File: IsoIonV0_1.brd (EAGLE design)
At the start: 41.9 x 27.9 mm, 56 parts, among them IC1 MCP3221, IC2 MCP4017-100K, IC4 TL072, IC5 TPS60400DBV

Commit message: Cleaned up sch small silkscreen adjustment on brd
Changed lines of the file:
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@@
 <wire x1="28.702" y1="22.606" x2="28.702" y2="19.558" width="0.8128" layer="21"/>
 <wire x1="28.702" y1="27.432" x2="28.702" y2="10.668" width="0.8128" layer="22" style="shortdash"/>
-<wire x1="28.702" y1="16.51" x2="28.702" y2="13.97" width="0.8128" layer="21" style="longdash"/>
+<wire x1="28.702" y1="16.51" x2="28.702" y2="14.224" width="0.8128" layer="21" style="longdash"/>
 </plain>
 <attributes>
@@
 </signal>
 </signals>
-<errors>
-</errors>
 </board>
 </drawing>

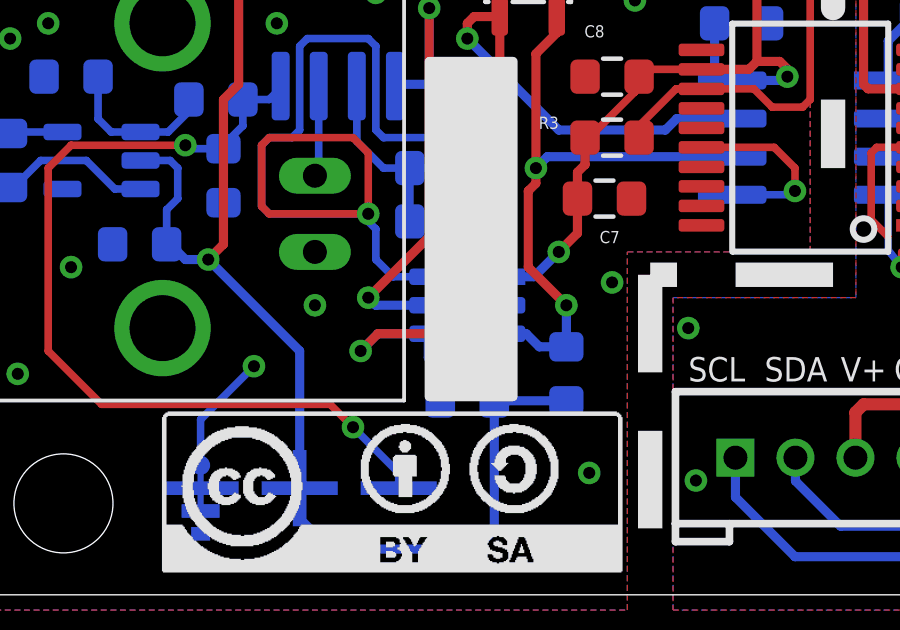
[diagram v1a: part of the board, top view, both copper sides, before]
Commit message: MCP4017 package updated to SC70-6
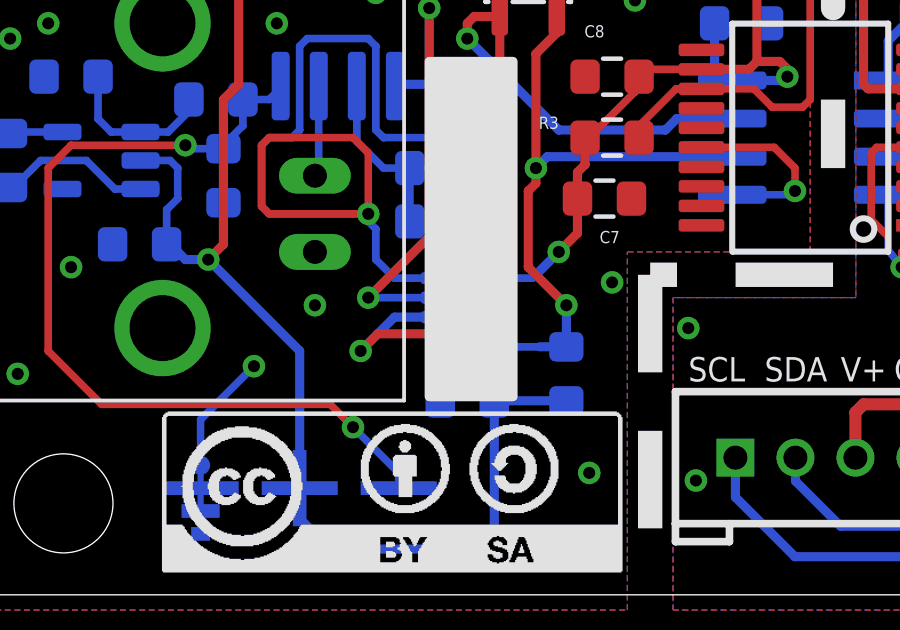
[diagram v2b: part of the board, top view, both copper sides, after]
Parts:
- IC2: device SW_DigitalAnalogICs:SOT23-6 -> SW_DigitalAnalogICs:SC70
- moved IC2 0.25 mm to (16.5, 9.91)
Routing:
- net ISOSDA: track 30.9 -> 31.8 mm
- net ISOSCL: track 20.8 -> 21.5 mm
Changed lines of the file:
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@@
 <attribute name="VALUE" x="16.764" y="27.305" size="0.4064" layer="28" rot="MR0"/>
 </element>
-<element name="IC2" library="SW_DigitalAnalogICs" package="SOT23-6" value="MCP4017-100K" x="16.51" y="9.652" smashed="yes" rot="MR270"/>
+<element name="IC2" library="SW_DigitalAnalogICs" package="SC70" value="MCP4017-100K" x="16.51" y="9.906" smashed="yes" rot="MR270"/>
 <element name="ISOIC1" library="SparkysWidgets" package="SO08" value="ADUM1250" x="27.94" y="15.24" smashed="yes" rot="MR270"/>
 <element name="ISOIC2" library="SparkysWidgets" package="SSOP20" value="ADUM6010" x="27.94" y="15.24" smashed="yes" rot="R90"/>
@@
 <wire x1="13.081" y1="12.573" x2="13.462" y2="12.192" width="0.254" layer="16"/>
 <wire x1="13.462" y1="12.192" x2="13.462" y2="11.176" width="0.254" layer="16"/>
-<wire x1="13.462" y1="11.176" x2="14.036" y2="10.602" width="0.254" layer="16"/>
-<wire x1="15.21" y1="10.602" x2="14.036" y2="10.602" width="0.254" layer="16"/>
+<wire x1="13.462" y1="11.176" x2="14.082" y2="10.556" width="0.254" layer="16"/>
 <wire x1="14.594" y1="12.446" x2="14.594" y2="12.076" width="0.254" layer="16"/>
-<wire x1="15.21" y1="10.602" x2="15.21" y2="10.638" width="0.254" layer="16"/>
-<wire x1="15.21" y1="10.638" x2="15.494" y2="10.922" width="0.254" layer="16"/>
+<wire x1="15.41" y1="10.556" x2="15.21" y2="10.638" width="0.254" layer="16"/>
 <wire x1="15.494" y1="10.922" x2="15.494" y2="14.224" width="0.254" layer="16"/>
 <wire x1="14.594" y1="12.446" x2="14.594" y2="14.224" width="0.254" layer="16"/>
@@
 <wire x1="12.7" y1="15.24" x2="13.208" y2="14.732" width="0.254" layer="1"/>
 <wire x1="13.208" y1="14.732" x2="13.208" y2="12.7" width="0.254" layer="1"/>
+<wire x1="15.41" y1="10.556" x2="14.082" y2="10.556" width="0.254" layer="16"/>
+<wire x1="15.21" y1="10.638" x2="15.494" y2="10.922" width="0.254" layer="16"/>
 </signal>
 <signal name="N$10">
@@
 <wire x1="16.394" y1="14.224" x2="16.394" y2="16.626" width="0.3048" layer="16"/>
 <wire x1="16.002" y1="17.018" x2="16.394" y2="16.626" width="0.3048" layer="16"/>
-<wire x1="15.21" y1="9.652" x2="13.462" y2="9.652" width="0.3048" layer="16"/>
-<wire x1="13.462" y1="9.652" x2="13.208" y2="9.906" width="0.3048" layer="16"/>
 <via x="13.208" y="9.906" extent="1-16" drill="0.4"/>
 <wire x1="13.208" y1="9.906" x2="15.24" y2="11.938" width="0.3048" layer="1"/>
@@
 <wire x1="15.24" y1="17.018" x2="14.157" y2="17.018" width="0.3048" layer="16"/>
 <wire x1="14.157" y1="17.018" x2="14.097" y2="16.958" width="0.3048" layer="16"/>
+<wire x1="15.41" y1="9.906" x2="13.208" y2="9.906" width="0.254" layer="16"/>
 </signal>
 <signal name="-5V">
@@
 <wire x1="17.399" y1="6.477" x2="16.256" y2="7.62" width="0.254" layer="16"/>
 <wire x1="16.256" y1="7.62" x2="16.256" y2="10.16" width="0.254" layer="16"/>
-<wire x1="16.256" y1="10.16" x2="16.698" y2="10.602" width="0.254" layer="16"/>
-<wire x1="17.81" y1="10.602" x2="16.698" y2="10.602" width="0.254" layer="16"/>
-<wire x1="17.81" y1="10.602" x2="18.73" y2="10.602" width="0.3048" layer="16"/>
 <wire x1="18.73" y1="10.602" x2="19.558" y2="11.43" width="0.3048" layer="16"/>
 <via x="19.558" y="11.43" extent="1-16" drill="0.4"/>
@@
 <wire x1="8.89" y1="20.066" x2="8.89" y2="17.018" width="0.3048" layer="1"/>
 <wire x1="8.89" y1="17.018" x2="8.382" y2="16.51" width="0.3048" layer="1"/>
+<wire x1="17.61" y1="10.556" x2="18.684" y2="10.556" width="0.254" layer="16"/>
+<wire x1="18.684" y1="10.556" x2="18.73" y2="10.602" width="0.254" layer="16"/>
+<wire x1="17.61" y1="10.556" x2="16.652" y2="10.556" width="0.254" layer="16"/>
+<wire x1="16.652" y1="10.556" x2="16.256" y2="10.16" width="0.254" layer="16"/>
 </signal>
 <signal name="N$4">
@@
 <contactref element="IC1" pad="4"/>
 <contactref element="IC2" pad="4"/>
-<wire x1="15.21" y1="8.702" x2="15.21" y2="7.904" width="0.3048" layer="16"/>
-<wire x1="15.21" y1="7.904" x2="15.61" y2="7.504" width="0.3048" layer="16"/>
+<wire x1="15.41" y1="7.704" x2="15.61" y2="7.504" width="0.3048" layer="16"/>
 <wire x1="15.61" y1="6.477" x2="15.61" y2="7.504" width="0.3048" layer="16"/>
 <wire x1="17.592" y1="19.274" x2="17.592" y2="11.084" width="0.3048" layer="1"/>
@@
 <wire x1="13.528" y1="8.702" x2="12.954" y2="8.128" width="0.3048" layer="1"/>
 <via x="12.954" y="8.128" extent="1-16" drill="0.4"/>
-<wire x1="15.21" y1="8.702" x2="13.528" y2="8.702" width="0.3048" layer="16"/>
-<wire x1="13.528" y1="8.702" x2="12.954" y2="8.128" width="0.3048" layer="16"/>
+<wire x1="14.082" y1="9.256" x2="12.954" y2="8.128" width="0.3048" layer="16"/>
 <wire x1="25.34" y1="15.875" x2="23.495" y2="15.875" width="0.3048" layer="16"/>
 <wire x1="23.495" y1="15.875" x2="23.114" y2="15.494" width="0.3048" layer="16"/>
@@
 <wire x1="17.592" y1="19.274" x2="16.734" y2="19.274" width="0.3048" layer="1"/>
 <wire x1="16.734" y1="19.274" x2="16.51" y2="19.05" width="0.3048" layer="1"/>
+<wire x1="15.41" y1="9.256" x2="14.082" y2="9.256" width="0.3048" layer="16"/>
+<wire x1="15.41" y1="9.256" x2="15.41" y2="7.704" width="0.3048" layer="16"/>
 </signal>
 <signal name="ISOSCL">
@@
 <contactref element="IC1" pad="5"/>
 <contactref element="IC2" pad="3"/>
-<wire x1="17.81" y1="8.702" x2="18.476" y2="8.702" width="0.3048" layer="16"/>
-<wire x1="18.476" y1="8.702" x2="18.912" y2="8.266" width="0.3048" layer="16"/>
 <wire x1="19.812" y1="8.266" x2="18.912" y2="8.266" width="0.3048" layer="16"/>
 <wire x1="25.34" y1="14.605" x2="19.177" y2="14.605" width="0.3048" layer="16"/>
@@
 <via x="19.812" y="9.652" extent="1-16" drill="0.4"/>
 <wire x1="19.812" y1="9.652" x2="19.812" y2="8.266" width="0.3048" layer="16"/>
+<wire x1="17.61" y1="9.256" x2="17.61" y2="8.806" width="0.254" layer="16"/>
+<wire x1="17.61" y1="8.806" x2="18.15" y2="8.266" width="0.254" layer="16"/>
+<wire x1="18.912" y1="8.266" x2="18.15" y2="8.266" width="0.254" layer="16"/>
 </signal>
 <signal name="N$6">
@@
 </signal>
 </signals>
+<errors>
+</errors>
 </board>
 </drawing>

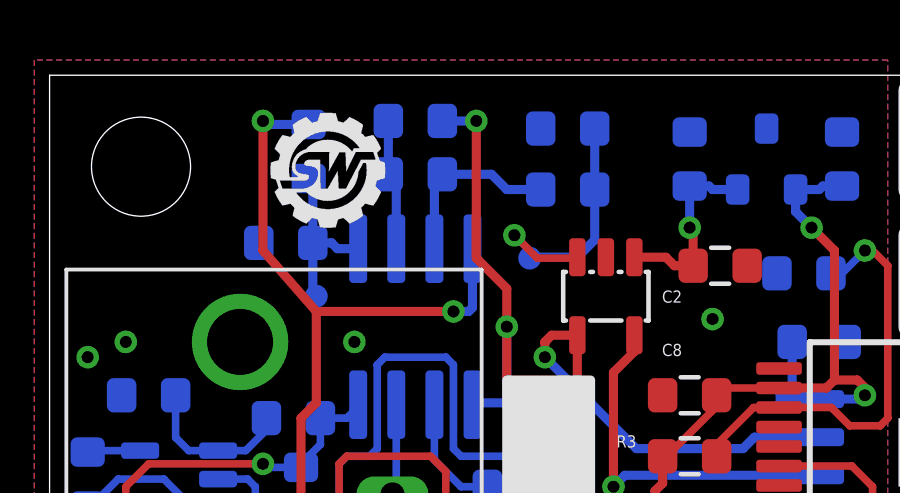
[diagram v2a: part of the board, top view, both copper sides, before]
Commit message: Routed Offset from VREF instead of VDD
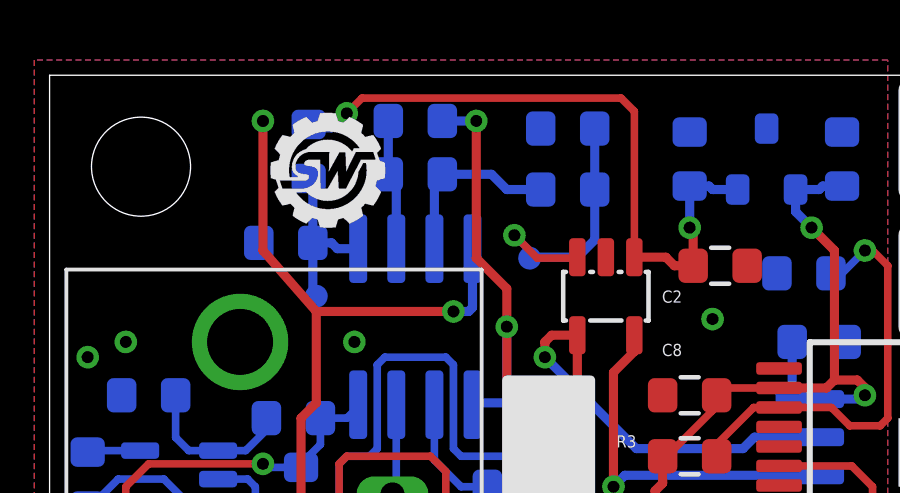
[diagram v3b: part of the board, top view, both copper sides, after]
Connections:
- net VDD: no longer R12.1
- net VREF: now also R12.1
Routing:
- net VREF: track 6.43 -> 22.8 mm, vias 1 -> 2
- net VDD: track 88.1 -> 86.6 mm
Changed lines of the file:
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@@
 <wire x1="21.452" y1="21.59" x2="21.452" y2="22.744" width="0.3048" layer="1"/>
 <wire x1="21.452" y1="22.744" x2="21.336" y2="22.86" width="0.3048" layer="1"/>
+<contactref element="R12" pad="1"/>
+<wire x1="19.492" y1="21.874" x2="19.492" y2="26.736" width="0.254" layer="1"/>
+<wire x1="19.492" y1="26.736" x2="19.05" y2="27.178" width="0.254" layer="1"/>
+<wire x1="19.05" y1="27.178" x2="10.414" y2="27.178" width="0.254" layer="1"/>
+<wire x1="10.414" y1="27.178" x2="9.906" y2="26.67" width="0.254" layer="1"/>
+<via x="9.906" y="26.67" extent="1-16" drill="0.4"/>
+<wire x1="9.906" y1="26.67" x2="9.398" y2="26.162" width="0.254" layer="16"/>
+<wire x1="9.398" y1="26.162" x2="8.774" y2="26.162" width="0.254" layer="16"/>
+<wire x1="8.774" y1="26.162" x2="8.636" y2="26.3" width="0.254" layer="16"/>
 </signal>
 <signal name="GNDA">
@@
 <contactref element="IC2" pad="1"/>
 <contactref element="IC4" pad="8"/>
-<contactref element="R12" pad="1"/>
-<wire x1="8.636" y1="26.3" x2="7.228" y2="26.3" width="0.3048" layer="16"/>
 <wire x1="7.228" y1="26.3" x2="7.112" y2="26.416" width="0.3048" layer="16"/>
 <via x="7.112" y="26.416" extent="1-16" drill="0.4"/>

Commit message: Removed unsed VDD trace
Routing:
- net VDD: track 86.6 -> 77.7 mm, vias 6 -> 5
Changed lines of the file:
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@@
 <via x="3.302" y="10.922" extent="1-16" drill="0.4"/>
 <via x="11.43" y="9.652" extent="1-16" drill="0.4"/>
-<via x="10.16" y="19.05" extent="1-16" drill="0.4"/>
+<via x="9.652" y="19.558" extent="1-16" drill="0.4"/>
 <via x="1.524" y="7.366" extent="1-16" drill="0.4"/>
 </signal>
@@
 <contactref element="IC2" pad="1"/>
 <contactref element="IC4" pad="8"/>
-<wire x1="7.228" y1="26.3" x2="7.112" y2="26.416" width="0.3048" layer="16"/>
-<via x="7.112" y="26.416" extent="1-16" drill="0.4"/>
-<wire x1="7.112" y1="26.416" x2="7.112" y2="22.098" width="0.3048" layer="1"/>
-<wire x1="7.112" y1="22.098" x2="8.89" y2="20.066" width="0.3048" layer="1"/>
 <via x="13.462" y="20.066" extent="1-16" drill="0.4"/>
 <wire x1="13.462" y1="20.066" x2="13.97" y2="20.066" width="0.3048" layer="16"/>
 <wire x1="14.097" y1="22.158" x2="14.097" y2="20.193" width="0.3048" layer="16"/>
 <wire x1="14.097" y1="20.193" x2="13.97" y2="20.066" width="0.3048" layer="16"/>
-<wire x1="13.462" y1="20.066" x2="8.89" y2="20.066" width="0.3048" layer="1"/>
 <wire x1="8.382" y1="11.684" x2="7.874" y2="11.176" width="0.3048" layer="1"/>
 <via x="7.874" y="11.176" extent="1-16" drill="0.4"/>
@@
 <wire x1="25.213" y1="17.018" x2="25.34" y2="17.145" width="0.3048" layer="16"/>
 <wire x1="8.382" y1="11.684" x2="8.382" y2="16.51" width="0.3048" layer="1"/>
-<wire x1="8.89" y1="20.066" x2="8.89" y2="17.018" width="0.3048" layer="1"/>
-<wire x1="8.89" y1="17.018" x2="8.382" y2="16.51" width="0.3048" layer="1"/>
 <wire x1="17.61" y1="10.556" x2="18.684" y2="10.556" width="0.254" layer="16"/>
 <wire x1="18.684" y1="10.556" x2="18.73" y2="10.602" width="0.254" layer="16"/>
 <wire x1="17.61" y1="10.556" x2="16.652" y2="10.556" width="0.254" layer="16"/>
 <wire x1="16.652" y1="10.556" x2="16.256" y2="10.16" width="0.254" layer="16"/>
+<wire x1="8.382" y1="16.51" x2="11.938" y2="20.066" width="0.3048" layer="1"/>
+<wire x1="11.938" y1="20.066" x2="13.462" y2="20.066" width="0.3048" layer="1"/>
 </signal>
 <signal name="N$4">
